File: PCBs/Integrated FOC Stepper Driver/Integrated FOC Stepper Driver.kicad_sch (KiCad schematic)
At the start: 65 parts, among them J1 INPUT, J2 USB C Receptacle, J3 OUTPUT, J4 MOTOR, J5 Conn_01x02, SW1 BOOT, SW2 RESET, U1 PJ54M50SE, U2 PJ9500M33SA, U3 RP2040, U4 W25Q128JVS, U5 SN65HVD1050D, U6 MT6701CT, Y1 12MHz/12pF/50Ω/20ppm

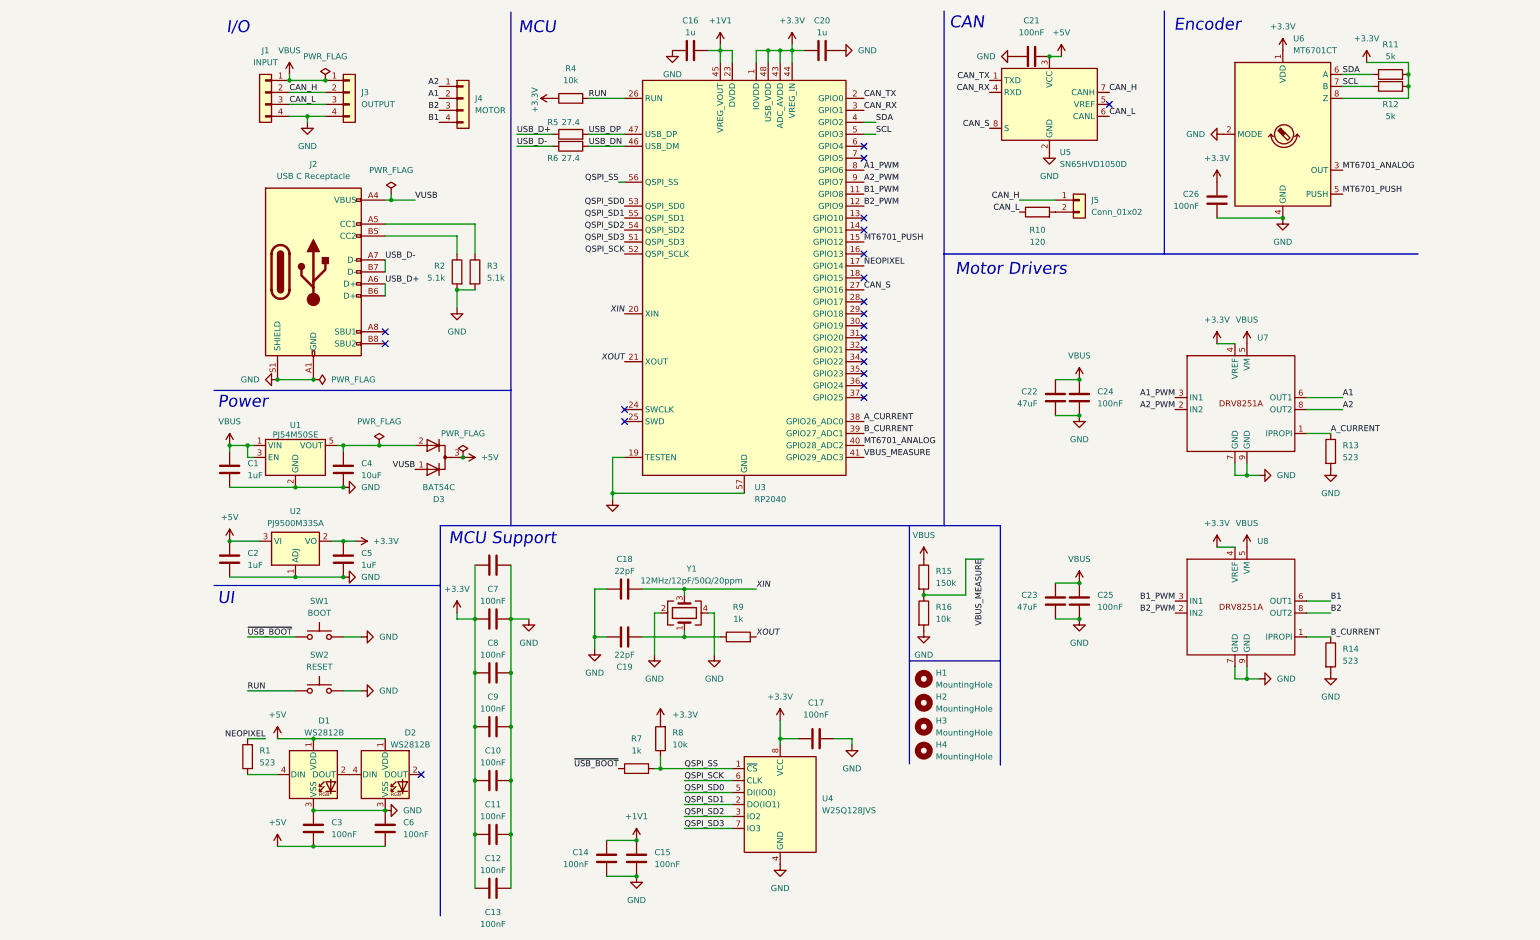
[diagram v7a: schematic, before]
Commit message: Start re-layout with advice from John
6-layer stackup:
- Power
- Ground
- Signal
- Signal
- Ground
- Power

Switching to oscillator recommended by RPi in Hardware Design guide

Switching to THT JST-XH connector for motor to allow motor controllers to sit next to the connector

Fixed I2C pullup resistor values

Moved RP2040 decoupling caps to hierarchical sheet

Add SWD debug port
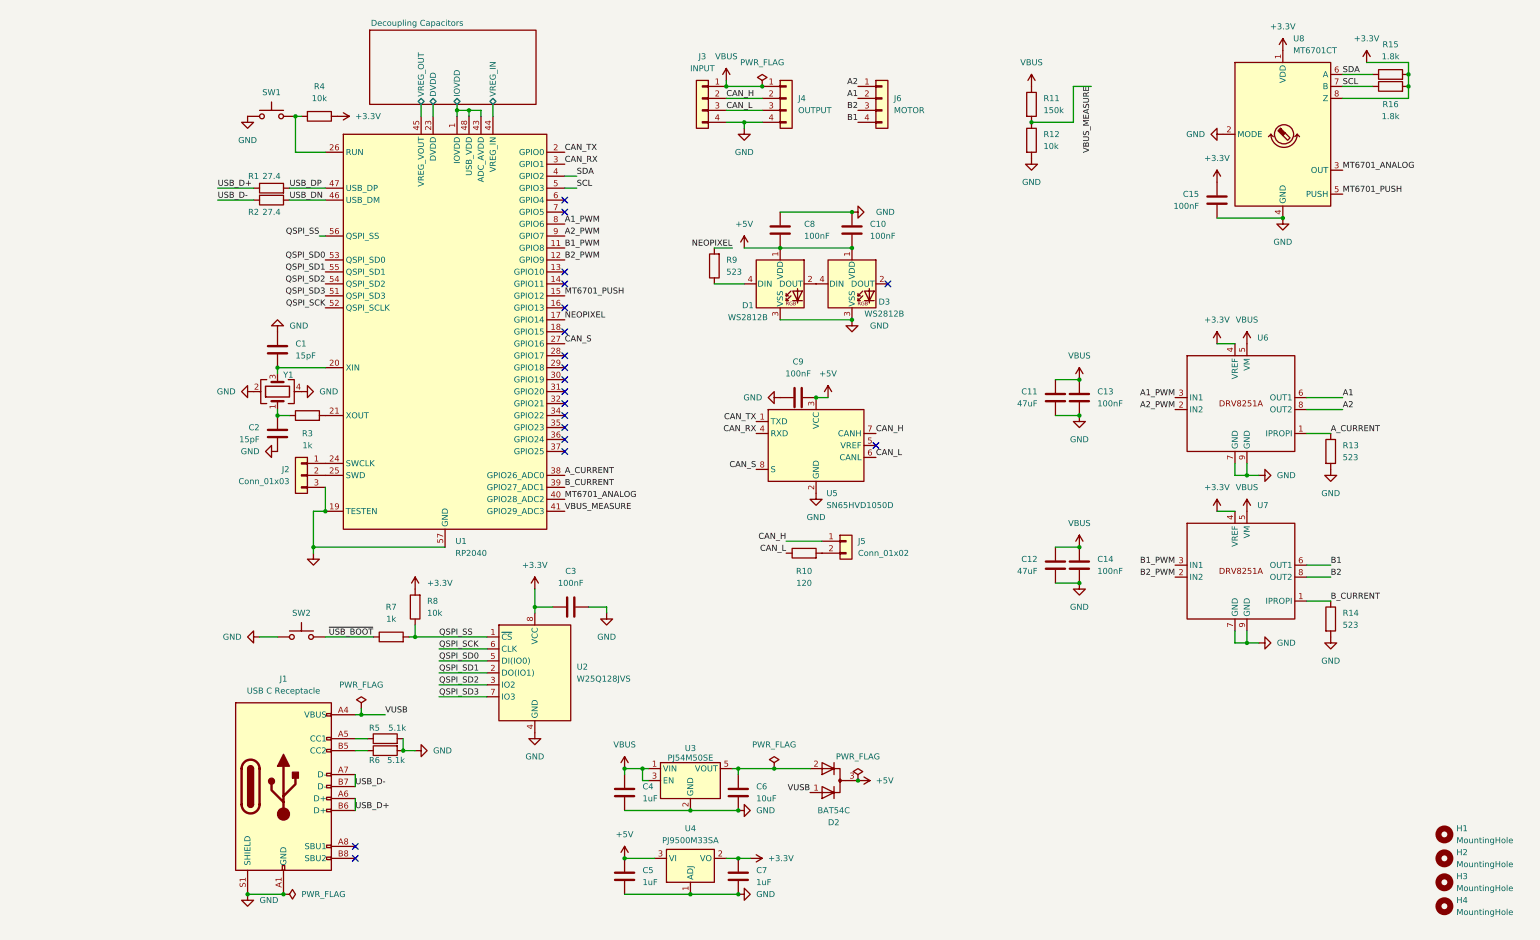
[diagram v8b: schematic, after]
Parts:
- removed C11, C12, C13, C14, C15, C3, C6, C7, C9: 100nF, Capacitor_SMD:C_0402_1005Metric, symbol Device:C
- removed C16, C20: 1u, Capacitor_SMD:C_0402_1005Metric, symbol Device:C
- added J2: Conn_01x03, Connector_PinHeader_2.54mm:PinHeader_1x03_P2.54mm_Vertical, symbol Connector_Generic:Conn_01x03
- C1: renamed from C18; value 22pF -> 15pF; LCSC C2185179 -> C18164617
- C10, C8: LCSC C307331 -> C960916
- C11: renamed from C22; LCSC C2932476 -> C5447693
- C12: renamed from C23; LCSC C2932476 -> C5447693
- C13: renamed from C24; LCSC C307331 -> C960916
- C14: renamed from C25; LCSC C307331 -> C960916
- C15: renamed from C26; LCSC C307331 -> C960916
- C2: renamed from C19; value 22pF -> 15pF; LCSC C2185179 -> C18164617
- C3: renamed from C17; LCSC C307331 -> C960916
- C4: renamed from C1; footprint Capacitor_SMD:C_0603_1608Metric -> Capacitor_SMD:C_0402_1005Metric; LCSC C15849 -> C1518208
- C5: renamed from C2; footprint Capacitor_SMD:C_0603_1608Metric -> Capacitor_SMD:C_0402_1005Metric; LCSC C15849 -> C1518208
- C7: renamed from C5; footprint Capacitor_SMD:C_0603_1608Metric -> Capacitor_SMD:C_0402_1005Metric; LCSC C15849 -> C1518208
- C9: renamed from C21; LCSC C307331 -> C960916
- J5: LCSC C706874 -> (none)
- J6: renamed from J4; footprint Connector_JST:JST_XH_S4B-XH-SM4-TB_1x04-1MP_P2.50mm_Horizontal -> Connector_JST:JST_XH_S4B-XH-A_1x04_P2.50mm_Horizontal
- R15: renamed from R11; value 5k -> 1.8k; LCSC C477765 -> C163481
- R16: renamed from R12; value 5k -> 1.8k; LCSC C477765 -> C163481
- R3: renamed from R9; LCSC C106235 -> C105637
- R5: renamed from R3; LCSC C2906948 -> C105872
- R6: renamed from R2; LCSC C2906948 -> C105872
- R7: LCSC C106235 -> C105637
- SW1: renamed from SW2; value RESET -> ~
- SW2: renamed from SW1; value BOOT -> ~
- Y1: value 12MHz/12pF/50Ω/20ppm -> ABM8-272-T3; LCSC C258938 -> C20625731
- renumbered C4 to C6, D3 to D2, D2 to D3, J2 to J1, J1 to J3, J3 to J4, R5 to R1, R15 to R11, R16 to R12, R6 to R2, R1 to R9, U3 to U1, U4 to U2, U1 to U3, U2 to U4, U7 to U6, U8 to U7, U6 to U8
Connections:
- net +3.3V: no longer C10.2, C8.2, U1.1 (IOVDD), U1.10 (IOVDD), U1.22 (IOVDD), U1.33 (IOVDD), U1.42 (IOVDD), U1.43 (ADC_AVDD), U1.44 (VREG_IN), U1.48 (USB_VDD), U1.49 (IOVDD)
- net +5V: now also C10.1, C8.1
- net GND: now also C1.2, C10.2, C8.2, SW1.2, J2.3 (Pin_3); no longer C1.1, C10.1, C8.1, SW1.1
- net at U1.24 (SWCLK): now also J2.1 (Pin_1)
- net at U1.25 (SWD): now also J2.2 (Pin_2)
- net +1V1 renamed Decoupling Capacitors/DVDD
- net Decoupling Capacitors/DVDD: no longer U1.45 (VREG_VOUT)
- net RUN: no longer names the net of R4.2, U1.26 (RUN)
- net RUN: now also SW1.1; no longer SW1.2
- net XIN: no longer names the net of U1.20 (XIN), Y1.3
- net XIN: now also C1.1; no longer C1.2
- net XOUT: no longer names the net of R3.2, U1.21 (XOUT)
- new net Decoupling Capacitors/IOVDD: U1.1 (IOVDD), U1.10 (IOVDD), U1.22 (IOVDD), U1.33 (IOVDD), U1.42 (IOVDD), U1.43 (ADC_AVDD), U1.48 (USB_VDD), U1.49 (IOVDD)
- new net Decoupling Capacitors/VREG_IN: U1.44 (VREG_IN)
- new net Decoupling Capacitors/VREG_OUT: U1.45 (VREG_VOUT)
- no-connect marks 21 -> 19
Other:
- added sheet Decoupling Capacitors (decoupling_caps.kicad_sch)
- note removed: "CAN"
- note removed: "Encoder"
- note removed: "I/O"
- note removed: "MCU"
- note removed: "MCU Support"
- note removed: "Motor Drivers"
- note removed: "Power"
- note removed: "UI"
- moved on the sheet: C1, C12, C14, C2, C3, C4, C5, C6, C7, C9, D1, D2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
